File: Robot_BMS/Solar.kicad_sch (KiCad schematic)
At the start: 19 parts, among them J4 691137710002, U2 LM3488MM, U3 CSD18563Q5A

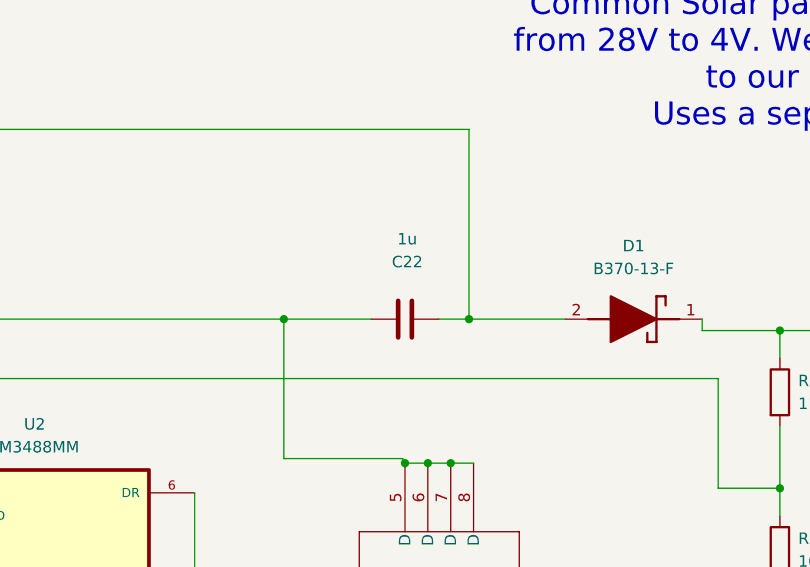
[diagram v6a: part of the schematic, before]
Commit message: still adding in symbols & footprints for passives
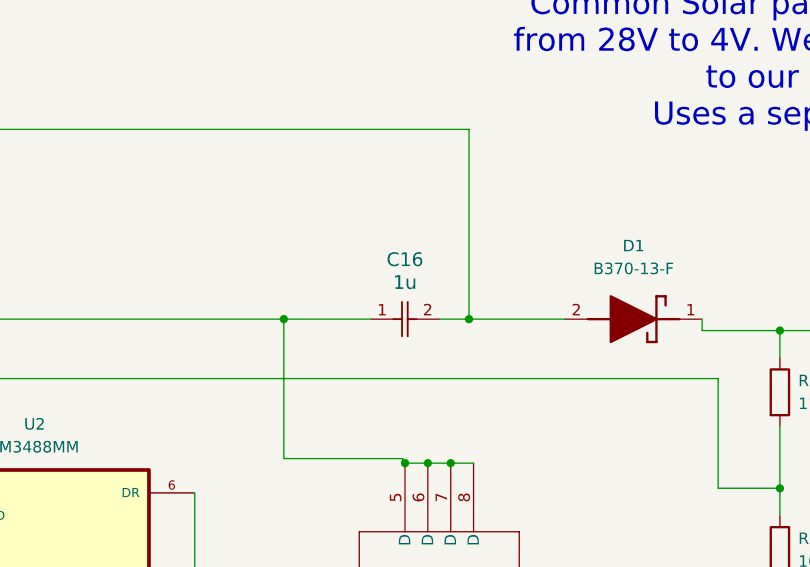
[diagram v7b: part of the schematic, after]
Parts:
- removed C22: 1u, symbol Device:C
- added C16: 1u, CAP_1608_TDK, symbol C1608X5R1H105K080AB:C1608X5R1H105K080AB
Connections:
- net at L2.1, U3.5 (D), U3.6 (D)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: now also C16.1
- net at D1.2 (A), L2.2: now also C16.2
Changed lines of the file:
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@@
+	)
+	(symbol
+		(lib_id "C1608X5R1H105K080AB:C1608X5R1H105K080AB")
+		(at 181.102 51.816 0)
+		(unit 1)
+		(exclude_from_sim no)
+		(in_bom yes)
+		(on_board yes)
+		(dnp no)
+		(fields_autoplaced yes)
+		(property "Reference" "C16"
+			(at 184.912 45.212 0)
+			(effects
+				(font
+					(size 1.524 1.524)
+				)
+			)
+		)
+		(property "Value" "1u"
+			(at 184.912 47.752 0)
+			(effects
+				(font
+					(size 1.524 1.524)
+				)
+			)
+		)
+		(property "Footprint" "CAP_1608_TDK"
+			(at 181.102 51.816 0)
+			(effects
+				(font
+					(size 1.27 1.27)
+					(italic yes)
+				)
+				(hide yes)
+			)
+		)
+		(property "Datasheet" "C1608X5R1H105K080AB"
+			(at 181.102 51.816 0)
+			(effects
+				(font
+					(size 1.27 1.27)
+					(italic yes)
+				)
+				(hide yes)
+			)
+		)
+		(property "Description" ""
+			(at 181.102 51.816 0)
+			(effects
+				(font
+					(size 1.27 1.27)
+				)
+				(hide yes)
+			)
+		)
+		(pin "1"
+		)
+		(pin "2"
+		)
+		(instances
+			(project "Robot_BMS"
+				(path "/72551b1c-3d40-4199-8911-e5b015f4abec/ff8c01d9-7d3c-4161-8f4f-7a8402a9daec"
+					(reference "C16")
+					(unit 1)
+				)
+			)
+		)
 	)
 	(symbol
@@
 					(unit 1)
 				)
-			)
-		)
-	)
-	(symbol
-		(lib_id "Device:C")
-		(at 184.912 51.816 270)
-		(unit 1)
-		(exclude_from_sim no)
-		(in_bom yes)
-		(on_board yes)
-		(dnp no)
-		(property "Reference" "C22"
-			(at 185.166 45.466 90)
-			(effects
-				(font
-					(size 1.27 1.27)
-				)
-			)
-		)
-		(property "Value" "1u"
-			(at 185.166 42.926 90)
-			(effects
-				(font
-					(size 1.27 1.27)
-				)
-			)
-		)
-		(property "Footprint" ""
-			(at 181.102 52.7812 0)
-			(effects
-				(font
-					(size 1.27 1.27)
-				)
-				(hide yes)
-			)
-		)
-		(property "Datasheet" "~"
-			(at 184.912 51.816 0)
-			(effects
-				(font
-					(size 1.27 1.27)
-				)
-				(hide yes)
-			)
-		)
-		(property "Description" "Unpolarized capacitor"
-			(at 184.912 51.816 0)
-			(effects
-				(font
-					(size 1.27 1.27)
-				)
-				(hide yes)
-			)
-		)
-		(pin "1"
-		)
-		(pin "2"
-		)
-		(instances
-			(project "Robot_BMS"
-				(path "/72551b1c-3d40-4199-8911-e5b015f4abec/ff8c01d9-7d3c-4161-8f4f-7a8402a9daec"
-					(reference "C22")
-					(unit 1)
-				)

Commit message: all symbols footprints & models added
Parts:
- removed C17: 4.7u, symbol Device:C
- removed C19: 990p, symbol Device:C
- removed C20: 180n, symbol Device:C
- removed C21: 820p, symbol Device:C
- removed C23: 22u, symbol Device:C
- removed R19: 20, symbol Device:R
- removed R20: 600, symbol Device:R
- removed R21: 40k2, symbol Device:R
- removed R22: 100, symbol Device:R
- removed R24: 110k, symbol Device:R
- removed R25: 10k, symbol Device:R
- added C17: 4.7u, RobotBMS:CAPC1608X120N, symbol ZRB18AR6YA475ME05L:ZRB18AR6YA475ME05L
- added C19: 1n, RobotBMS:CAPRR254W50L508T317H508, symbol SR201A102JARTR1:SR201A102JARTR1
- added C20: 180n, RobotBMS:CAPC1608X90, symbol CC0603KRX7R6BB184:CC0603KRX7R6BB184
- added C21: 820p, RobotBMS:CAPC17795_95N_KEM, symbol C0603X821K5RACTU:C0603X821K5RACTU
- added C23, C24: 10u, RobotBMS:CAPC1608X90N, symbol CL10A106MA8NRNC:CL10A106MA8NRNC
- added R19: 20, RobotBMS:RES_ERJPA3F20R0V, symbol ERJPA3F20R0V:ERJPA3F20R0V
- added R20: 604, RobotBMS:RESC1508X50N, symbol CRCW0603604RFKEA:CRCW0603604RFKEA
- added R21: 40k2, RobotBMS:RESC1608X55N, symbol CRCW060340K2FKEAHP:CRCW060340K2FKEAHP
- added R22: 100, RobotBMS:RESC1608X55N, symbol AT0603DRE07100RL:AT0603DRE07100RL
- added R24: 110k, RobotBMS:RESC1608X55N, symbol CRCW0603110KFKEAC:CRCW0603110KFKEAC
- added R25: 10k, RobotBMS:RC0603N_YAG, symbol RC0603FR-0710KL:RC0603FR-0710KL
- C18: renamed from C14; footprint CAPC17595_87N_KEM -> RobotBMS:CAPC17595_87N_KEM
- C22: renamed from C16; footprint CAP_1608_TDK -> RobotBMS:CAP_1608_TDK
- R23: footprint (none) -> RobotBMS:RESC1508X50N
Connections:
- net DR_Source: now also R22.1
- net GND: now also C17.1, C19.1, C20.2, C21.2, C23.1, C24.1, R21.1, R25.1
- net Isense: now also C21.1, R22.2
- net SOLAR_15V_OUT: now also C23.2, C24.2, R24.2
- net SOLAR_VIN: now also C17.2, R19.2
- net at U2.2 (COMP): now also C19.2, R20.2
- net at U2.3 (FB): now also R24.1, R25.2
- net at U2.7 (FA/SYNC/SD): now also R21.2
- net at C18.1, U2.8 (VIN): now also R19.1
- new net: C20.1, R20.1
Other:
- moved on the sheet: C18
